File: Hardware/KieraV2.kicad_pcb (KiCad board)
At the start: 2 copper layers, 111 x 63.2 mm, 110 parts, among them J1 Conn_01x04_Male, J2 Conn_01x06_Male, SW1 SW_Rotary2x4, SW10 SW_Push, SW11 SW_Push, SW2 SW_Rotary2x4, SW3 SW_Push, SW4 SW_Push, SW5 SW_Push, SW6 SW_Push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

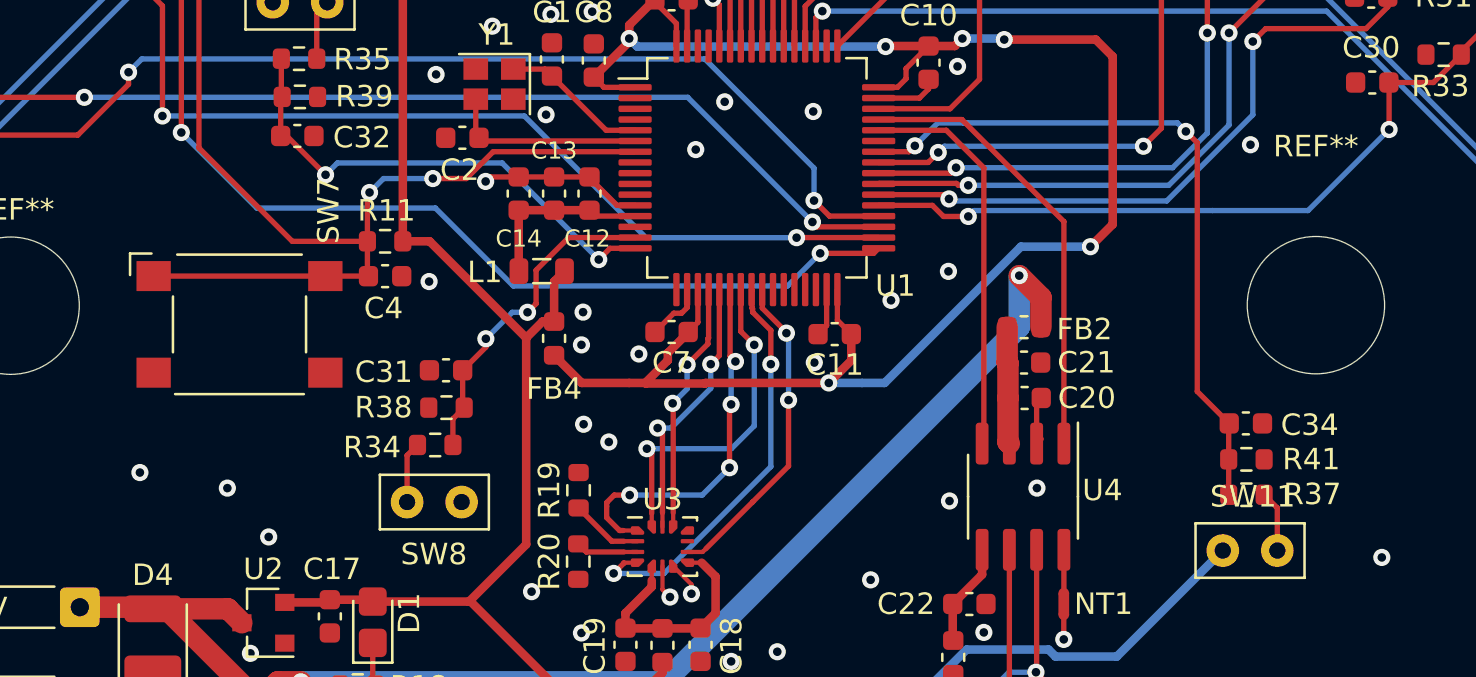
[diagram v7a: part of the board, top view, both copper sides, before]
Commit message: refilled zones
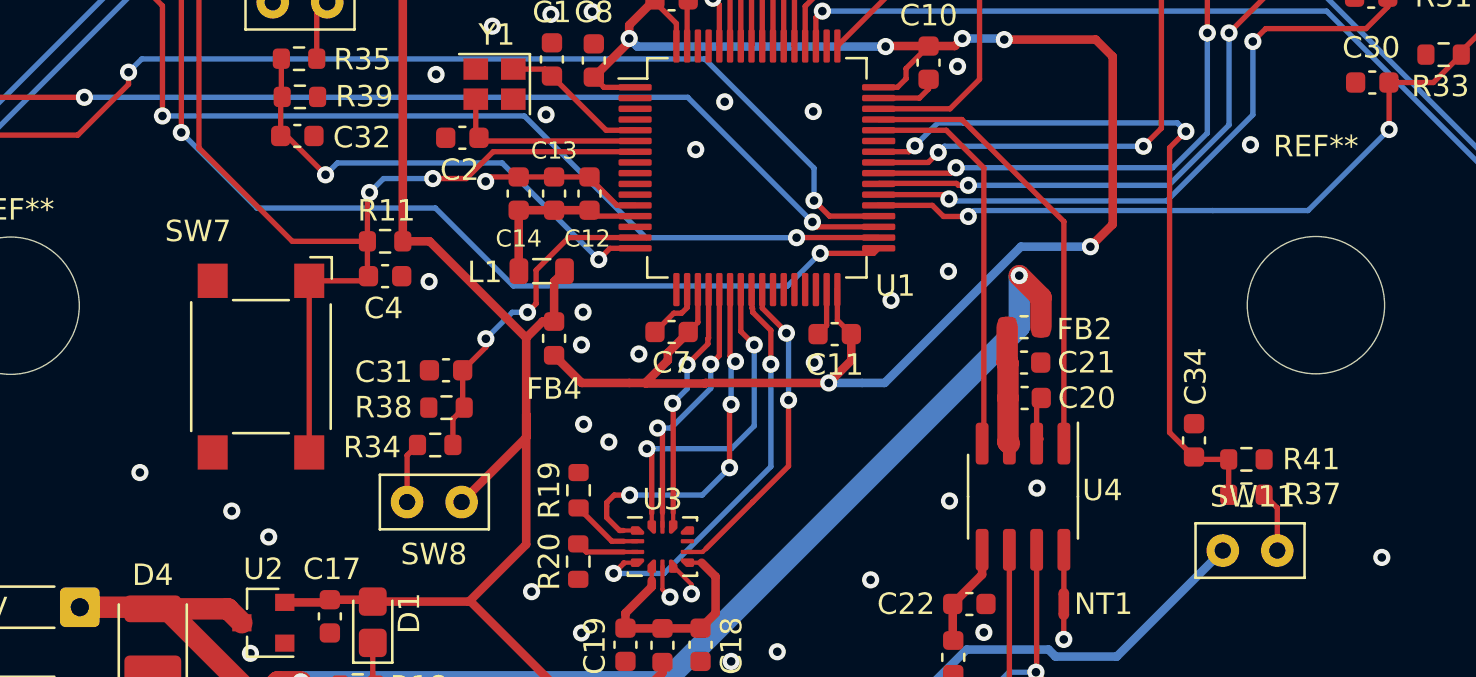
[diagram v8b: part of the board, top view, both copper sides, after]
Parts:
- moved C34 2.54 mm to (182.8, 122.1), turned to 90 degrees
- moved SW7 2.21 mm to (139.3, 118.6), turned to 270 degrees
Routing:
- net +3V3: track 275.0 -> 280.3 mm
- net /SW10: track 33.0 -> 34.5 mm
- net /NRST: track 52.9 -> 53.7 mm
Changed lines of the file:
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@@
     (thickness 1.6)
     (drawings 31)
-    (tracks 763)
+    (tracks 767)
     (zones 0)
     (modules 110)
@@
   )
   (module Capacitor_SMD:C_0603_1608Metric (layer F.Cu)
-    (at 185.185 121.285)
+    (at 182.77 122.075 90)
     (descr "Capacitor SMD 0603 (1608 Metric), square (rectangular) end terminal, IPC_7351 nominal, (Body size source: IPC-SM-782 page 76, https://www.pcb-3d.com/wordpress/wp-content/uploads/ipc-sm-782a_amendment_1_and_2.pdf), generated with kicad-footprint-generator")
     (tags capacitor)
     (attr smd)
-    (fp_text reference C34 (at 2.975 0.075) (layer F.SilkS)
+    (fp_text reference C34 (at 2.975 0.075 90) (layer F.SilkS)
       (effects (font (size 1 1) (thickness 0.15)))
     )
-    (fp_text value 100nF (at 0 1.43) (layer F.Fab)
+    (fp_text value 100nF (at 0 1.43 90) (layer F.Fab)
       (effects (font (size 1 1) (thickness 0.15)))
     )
-    (fp_text user %R (at 0 0) (layer F.Fab)
+    (fp_text user %R (at 0 0 90) (layer F.Fab)
       (effects (font (size 0.4 0.4) (thickness 0.06)))
     )
@@
     (fp_line (start 1.48 -0.73) (end 1.48 0.73) (layer F.CrtYd) (width 0.05))
     (fp_line (start 1.48 0.73) (end -1.48 0.73) (layer F.CrtYd) (width 0.05))
-    (pad 2 smd roundrect (at 0.775 0) (size 0.9 0.95) (layers F.Cu F.Paste F.Mask) (roundrect_rratio 0.25)
+    (pad 2 smd roundrect (at 0.775 0 90) (size 0.9 0.95) (layers F.Cu F.Paste F.Mask) (roundrect_rratio 0.25)
       (net 1 GND))
-    (pad 1 smd roundrect (at -0.775 0) (size 0.9 0.95) (layers F.Cu F.Paste F.Mask) (roundrect_rratio 0.25)
+    (pad 1 smd roundrect (at -0.775 0 90) (size 0.9 0.95) (layers F.Cu F.Paste F.Mask) (roundrect_rratio 0.25)
       (net 90 /SW10))
     (model ${KISYS3DMOD}/Capacitor_SMD.3dshapes/C_0603_1608Metric.wrl
@@
   )
   (module Button_Switch_SMD:SW_SPST_Omron_B3FS-100xP (layer F.Cu)
-    (at 138.29 116.67)
+    (at 139.29 118.64 270)
     (descr "Surface Mount Tactile Switch for High-Density Mounting, 3.1mm height, https://omronfs.omron.com/en_US/ecb/products/pdf/en-b3fs.pdf")
     (tags "Tactile Switch")
     (attr smd)
-    (fp_text reference SW7 (at 4.15 -5.3 -90) (layer F.SilkS)
+    (fp_text reference SW7 (at -6.31 2.93 180) (layer F.SilkS)
       (effects (font (size 1 1) (thickness 0.15)))
     )
-    (fp_text value SW_MEC_5G (at 0 4.2) (layer F.Fab)
+    (fp_text value SW_MEC_5G (at 0 4.2 90) (layer F.Fab)
       (effects (font (size 1 1) (thickness 0.15)))
     )
@@
     (fp_line (start -5.1 -2.3) (end -5.1 -3.3) (layer F.SilkS) (width 0.12))
     (fp_line (start -5.1 -3.3) (end -4.1 -3.3) (layer F.SilkS) (width 0.12))
-    (fp_text user %R (at 0 -2.2) (layer F.Fab)
+    (fp_text user %R (at 0 -2.2 90) (layer F.Fab)
       (effects (font (size 1 1) (thickness 0.15)))
     )
-    (pad 3 smd rect (at -4 2.25 180) (size 1.6 1.4) (layers F.Cu F.Paste F.Mask)
+    (pad 3 smd rect (at -4 2.25 90) (size 1.6 1.4) (layers F.Cu F.Paste F.Mask)
       (net 1 GND))
-    (pad 4 smd rect (at 4 2.25 180) (size 1.6 1.4) (layers F.Cu F.Paste F.Mask)
+    (pad 4 smd rect (at 4 2.25 90) (size 1.6 1.4) (layers F.Cu F.Paste F.Mask)
       (net 1 GND))
-    (pad 1 smd rect (at -4 -2.25 180) (size 1.6 1.4) (layers F.Cu F.Paste F.Mask)
+    (pad 1 smd rect (at -4 -2.25 90) (size 1.6 1.4) (layers F.Cu F.Paste F.Mask)
       (net 5 /NRST))
-    (pad 2 smd rect (at 4 -2.25 180) (size 1.6 1.4) (layers F.Cu F.Paste F.Mask)
+    (pad 2 smd rect (at 4 -2.25 90) (size 1.6 1.4) (layers F.Cu F.Paste F.Mask)
       (net 5 /NRST))
     (model ${KISYS3DMOD}/Button_Switch_SMD.3dshapes/SW_SPST_Omron_B3FS-100xP.wrl
@@
   (via (at 147.125 114.675) (size 0.8) (drill 0.4) (layers F.Cu B.Cu) (net 1))
   (via (at 139.65 126.575) (size 0.8) (drill 0.4) (layers F.Cu B.Cu) (net 1))
-  (via (at 137.725 124.3) (size 0.8) (drill 0.4) (layers F.Cu B.Cu) (net 1))
+  (via (at 137.93 125.37) (size 0.8) (drill 0.4) (layers F.Cu B.Cu) (net 1))
   (via (at 134.225 134.35) (size 0.8) (drill 0.4) (layers F.Cu B.Cu) (net 1))
   (via (at 137.075 136.5) (size 0.8) (drill 0.4) (layers F.Cu B.Cu) (net 1))
@@
   (segment (start 156.725 108.625) (end 150.111996 108.625) (width 0.25) (layer F.Cu) (net 5))
   (segment (start 144.295 114.42) (end 144.3 114.425) (width 0.25) (layer F.Cu) (net 5))
-  (segment (start 142.29 114.42) (end 144.295 114.42) (width 0.25) (layer F.Cu) (net 5))
-  (segment (start 142.29 114.42) (end 134.29 114.42) (width 0.25) (layer F.Cu) (net 5))
+  (segment (start 144.085 114.64) (end 144.3 114.425) (width 0.25) (layer F.Cu) (net 5))
+  (segment (start 141.54 114.64) (end 144.085 114.64) (width 0.25) (layer F.Cu) (net 5))
+  (segment (start 141.54 114.64) (end 141.54 122.64) (width 0.25) (layer F.Cu) (net 5))
   (segment (start 201.175 115.4) (end 201.15 115.425) (width 0.25) (layer F.Cu) (net 6))
   (segment (start 201.175 113.825) (end 201.175 115.4) (width 0.25) (layer F.Cu) (net 6))
@@
   (segment (start 152.4125 116.5375) (end 151.65 117.3) (width 0.4) (layer F.Cu) (net 8))
   (segment (start 151.65 126.925) (end 148.9875 129.5875) (width 0.4) (layer F.Cu) (net 8))
-  (segment (start 151.65 117.3) (end 151.65 126.925) (width 0.4) (layer F.Cu) (net 8))
   (segment (start 148.9875 129.5875) (end 144.5 129.5875) (width 0.4) (layer F.Cu) (net 8))
   (segment (start 147.15 112.8) (end 151.65 117.3) (width 0.4) (layer F.Cu) (net 8))
@@
   (segment (start 152.95 114.675) (end 153.435 114.19) (width 0.4) (layer F.Cu) (net 8))
   (segment (start 152.95 116.5375) (end 152.95 114.675) (width 0.4) (layer F.Cu) (net 8))
+  (segment (start 151.65 121.94) (end 151.65 120.87) (width 0.4) (layer F.Cu) (net 8))
+  (segment (start 148.64 124.95) (end 151.65 121.94) (width 0.4) (layer F.Cu) (net 8))
+  (segment (start 151.65 120.87) (end 151.65 126.925) (width 0.4) (layer F.Cu) (net 8))
+  (segment (start 151.65 117.3) (end 151.65 120.87) (width 0.4) (layer F.Cu) (net 8))
   (segment (start 134.175 129.85) (end 134.25 129.925) (width 1) (layer F.Cu) (net 9))
   (segment (start 130.85 129.85) (end 134.175 129.85) (width 1) (layer F.Cu) (net 9))
@@
   (segment (start 170.85 108.66) (end 170.385 109.125) (width 0.25) (layer F.Cu) (net 89))
   (segment (start 184.385 124.61) (end 184.385 122.96) (width 0.25) (layer F.Cu) (net 90))
-  (segment (start 184.385 121.31) (end 184.41 121.285) (width 0.25) (layer F.Cu) (net 90))
-  (segment (start 184.385 122.96) (end 184.385 121.31) (width 0.25) (layer F.Cu) (net 90))
   (via (at 182.39 107.68) (size 0.8) (drill 0.4) (layers F.Cu B.Cu) (net 90))
   (segment (start 182.39 107.68) (end 181.990001 107.280001) (width 0.25) (layer B.Cu) (net 90))
-  (segment (start 182.92 108.21) (end 182.39 107.68) (width 0.25) (layer F.Cu) (net 90))
-  (segment (start 182.92 119.795) (end 182.92 108.21) (width 0.25) (layer F.Cu) (net 90))
-  (segment (start 184.41 121.285) (end 182.92 119.795) (width 0.25) (layer F.Cu) (net 90))
   (via (at 169.76 108.35) (size 0.8) (drill 0.4) (layers F.Cu B.Cu) (net 90))
   (segment (start 169.485 108.625) (end 169.76 108.35) (width 0.25) (layer F.Cu) (net 90))
@@
   (segment (start 172.190001 107.280001) (end 171.999999 107.280001) (width 0.25) (layer B.Cu) (net 90))
   (segment (start 181.990001 107.280001) (end 172.190001 107.280001) (width 0.25) (layer B.Cu) (net 90))
+  (segment (start 182.88 122.96) (end 182.77 122.85) (width 0.25) (layer F.Cu) (net 90))
+  (segment (start 184.385 122.96) (end 182.88 122.96) (width 0.25) (layer F.Cu) (net 90))
+  (segment (start 181.63 108.44) (end 182.39 107.68) (width 0.25) (layer F.Cu) (net 90))
+  (segment (start 181.63 121.71) (end 181.63 108.44) (width 0.25) (layer F.Cu) (net 90))
+  (segment (start 182.77 122.85) (end 181.63 121.71) (width 0.25) (layer F.Cu) (net 90))
   (segment (start 114.34 99.625) (end 114.015 99.95) (width 0.25) (layer F.Cu) (net 91))
   (segment (start 117.45 99.625) (end 114.34 99.625) (width 0.25) (layer F.Cu) (net 91))
